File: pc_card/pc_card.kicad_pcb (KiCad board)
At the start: 4 copper layers, 64.8 x 47.5 mm, 59 parts, among them IC1 SV 3.3V, IC3 SV 4.5V, IC4 TPA152DR, J1 PCMCIA Connector, J2 Headphones Out, J3 SPI, U1 Z8601720ASG, U2 93CxxC, U3 YMF289B-S, U4 YAC516-E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

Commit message: up
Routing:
- net Net-(U3-DO): track 38.0 -> 31.5 mm
- net AGND: track 228.7 -> 234.5 mm, vias 119 -> 133
- net LRO: track 38.7 -> 40.7 mm
- net CLKO: track 33.5 -> 35.4 mm
- net BCO: track 35.0 -> 35.7 mm
- net ICS0#: track 65.7 -> 66.0 mm, vias 2 -> 3

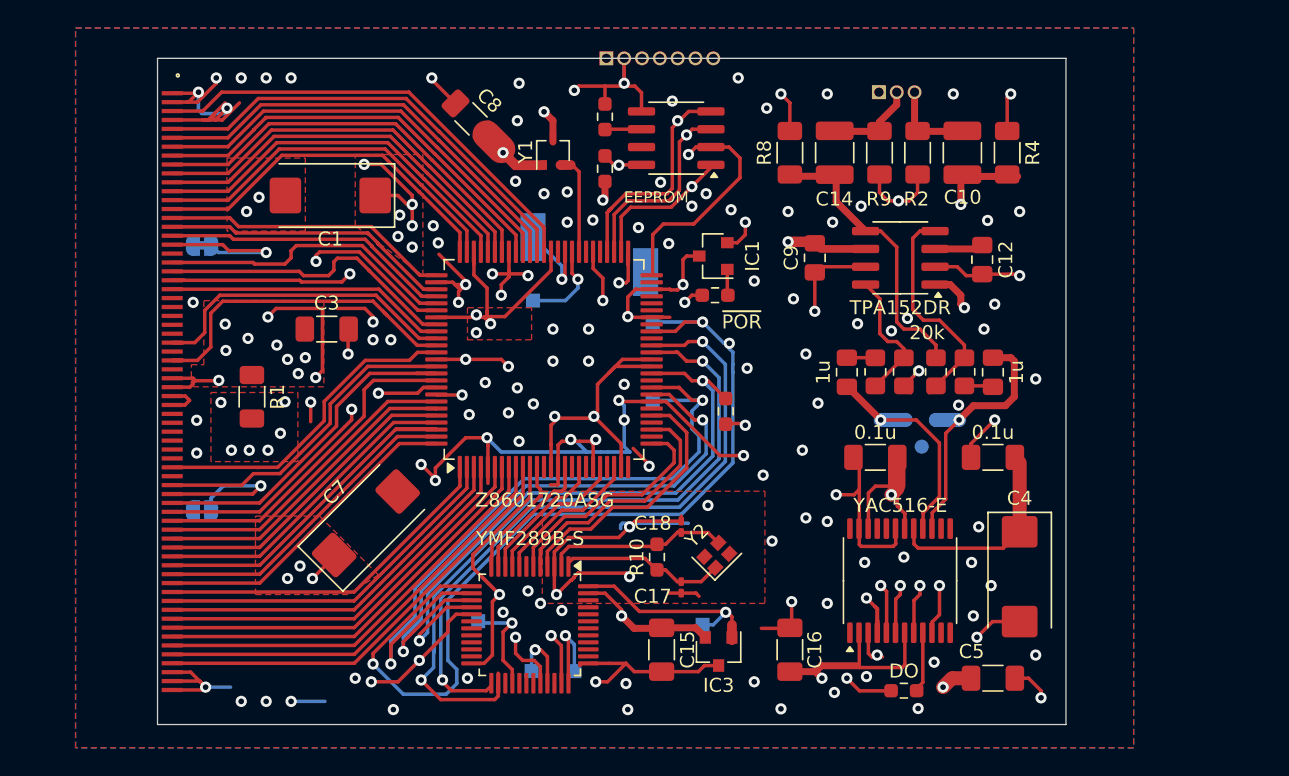
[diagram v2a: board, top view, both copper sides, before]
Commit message: hw rev3
* reDfMing the card so the connector can be assembled easier
* added software and specs
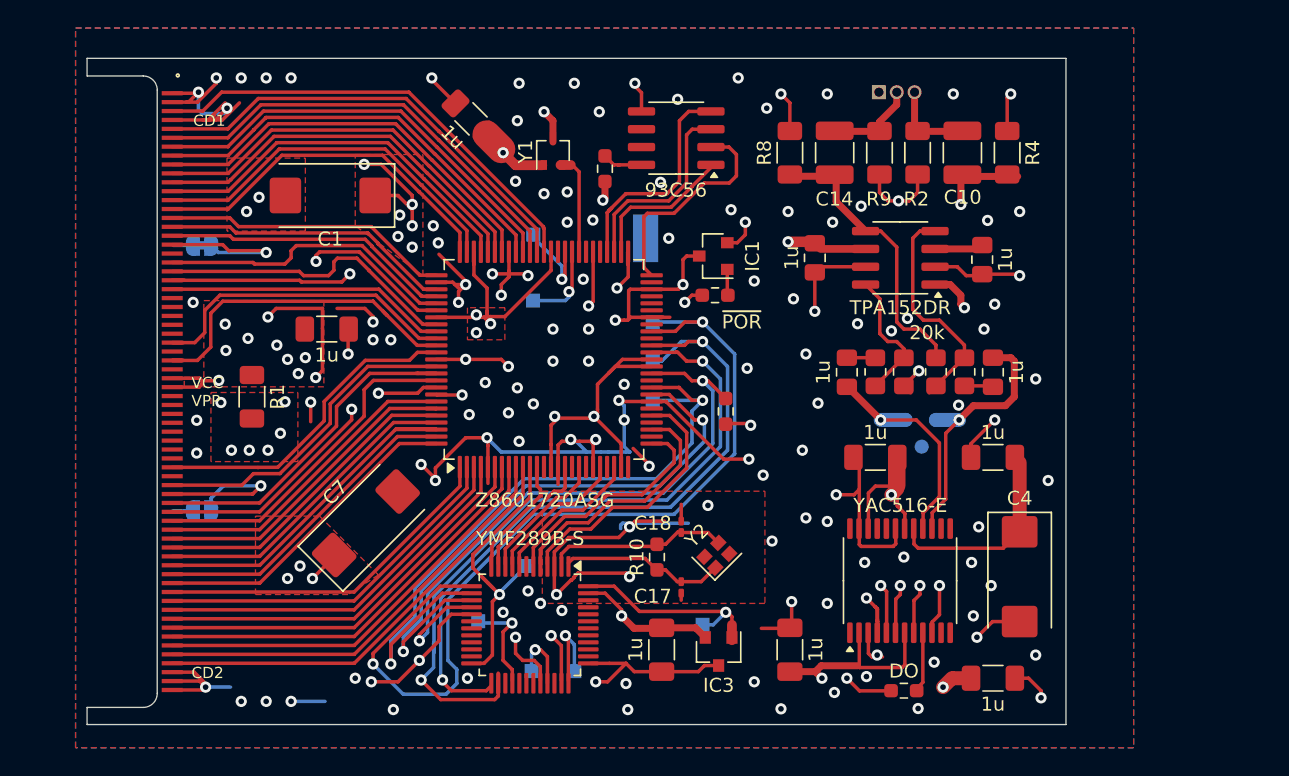
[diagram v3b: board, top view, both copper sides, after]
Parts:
- removed J3: SPI, Connector_PinHeader_1.27mm:PinHeader_1x07_P1.27mm_Vertical
- removed R13: ORG, Resistor_SMD:R_0603_1608Metric_Pad0.98x0.95mm_HandSolder
- added TP13: A0, TestPoint:TestPoint_Pad_1.0x1.0mm, B.Cu at (138.6, 78.9)
- added TP14: ~{RESET}, TestPoint:TestPoint_Pad_1.0x1.0mm, B.Cu at (129.5, 93.5)
- C15, C16, C2, C3, C5, C6, C8: value 0.1u -> 1u
- R11: value IRQ -> 20k
- TP7: footprint TestPoint:TestPoint_Keystone_5015_Micro-Minature -> TestPoint:TestPoint_Pad_1.0x1.0mm
- U2: value 93CxxC -> 93C56
- moved TP5 2.41 mm to (138.0, 70.1)
- moved TP7 0.18 mm to (130.0, 69.8)
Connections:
- U2 pad 6: Net-(U2-ORG) -> AGND
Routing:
- net POR#: track 30.1 -> 12.5 mm
- net EE_CS: track 20.5 -> 10.5 mm, vias 1 -> 0
- net AGND: track 234.5 -> 225.3 mm
- net EE_SK: track 24.2 -> 15.8 mm, vias 1 -> 0
- net VPP: track 10.4 -> 2.89 mm, vias 1 -> 0
- net EE_DO: track 20.3 -> 14.1 mm, vias 1 -> 0
- net EE_DI: track 22.0 -> 16.0 mm, vias 1 -> 0
- net IA0: track 47.2 -> 51.1 mm
- net ATA_HRESET#: track 51.8 -> 54.6 mm
- net (no net): track 2.74 -> 0.00 mm
- net Net-(U2-ORG): track 2.58 -> 0.00 mm
- net VCC: track 275.0 -> 277.3 mm
- net IRD#: track 50.6 -> 49.6 mm
- net IWR#: track 42.7 -> 42.0 mm
- net IIRQ#: track 44.7 -> 44.1 mm
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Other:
- board size 64.8 x 47.5 mm -> 69.8 x 47.5 mm
- board text added: "CD1"
- board text added: "CD2"
- board text added: "HW rev.3"
- board text added: "VCC VPP"
- board text removed: "HW rev.2"
- board text removed: "VPP GND DI DO SK CS ~{RES}"

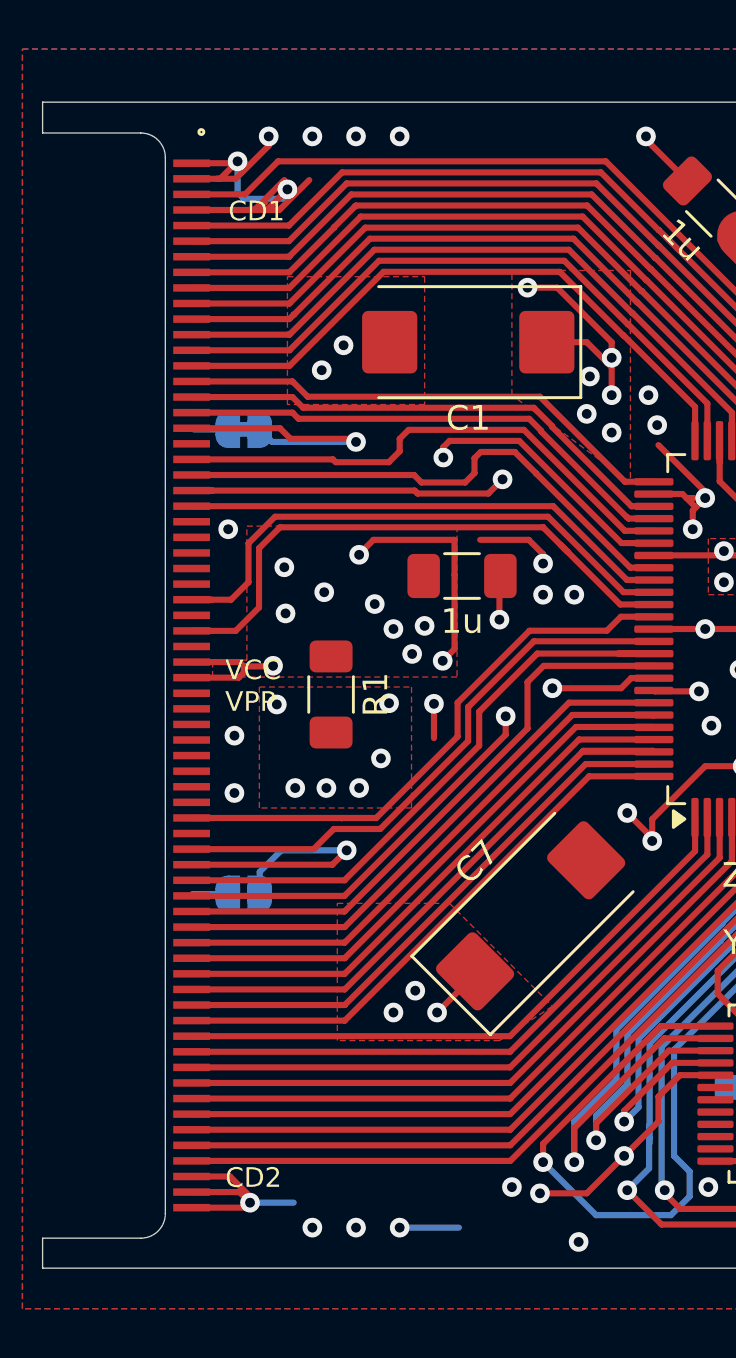
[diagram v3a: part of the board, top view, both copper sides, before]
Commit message: fiddling with connector
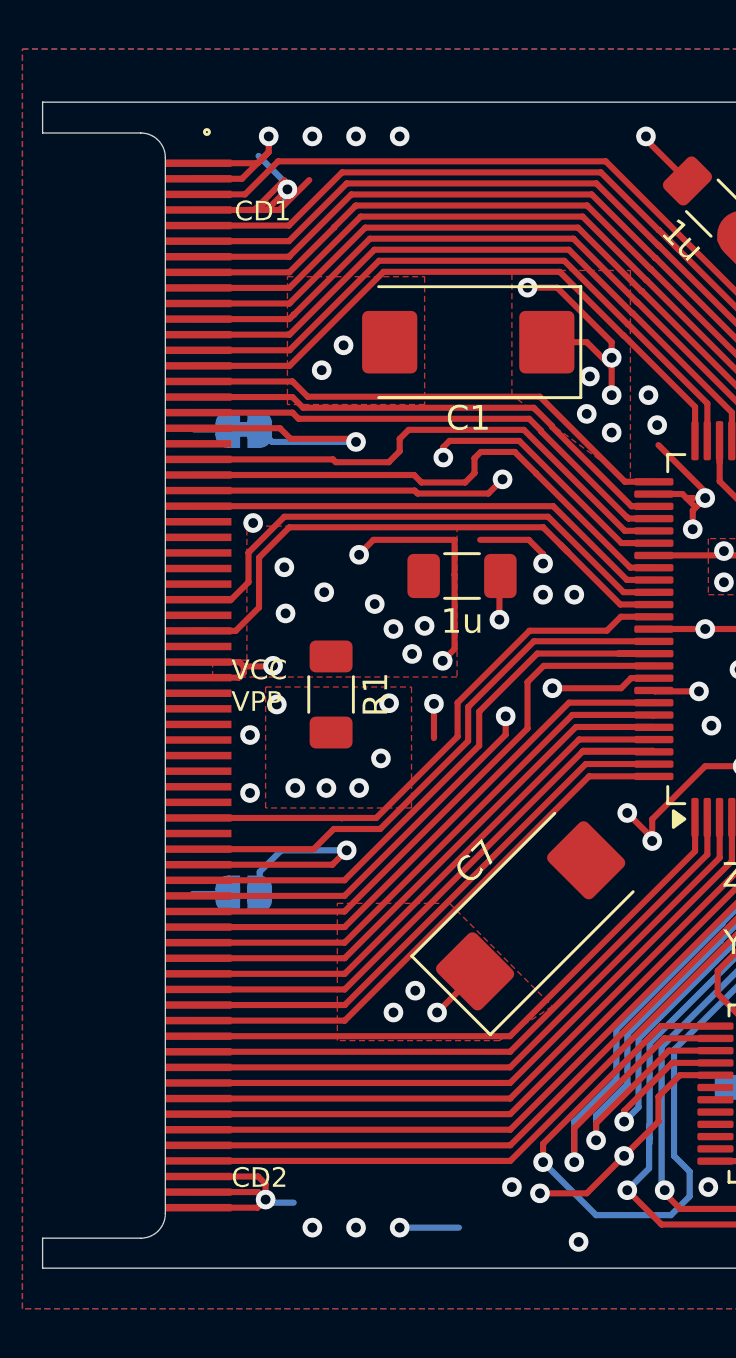
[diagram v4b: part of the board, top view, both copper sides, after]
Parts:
- moved J1 0.23 mm to (104.5, 59.8)
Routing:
- net WE#: track 23.3 -> 21.4 mm
- net AGND: track 225.3 -> 226.2 mm, vias 133 -> 132

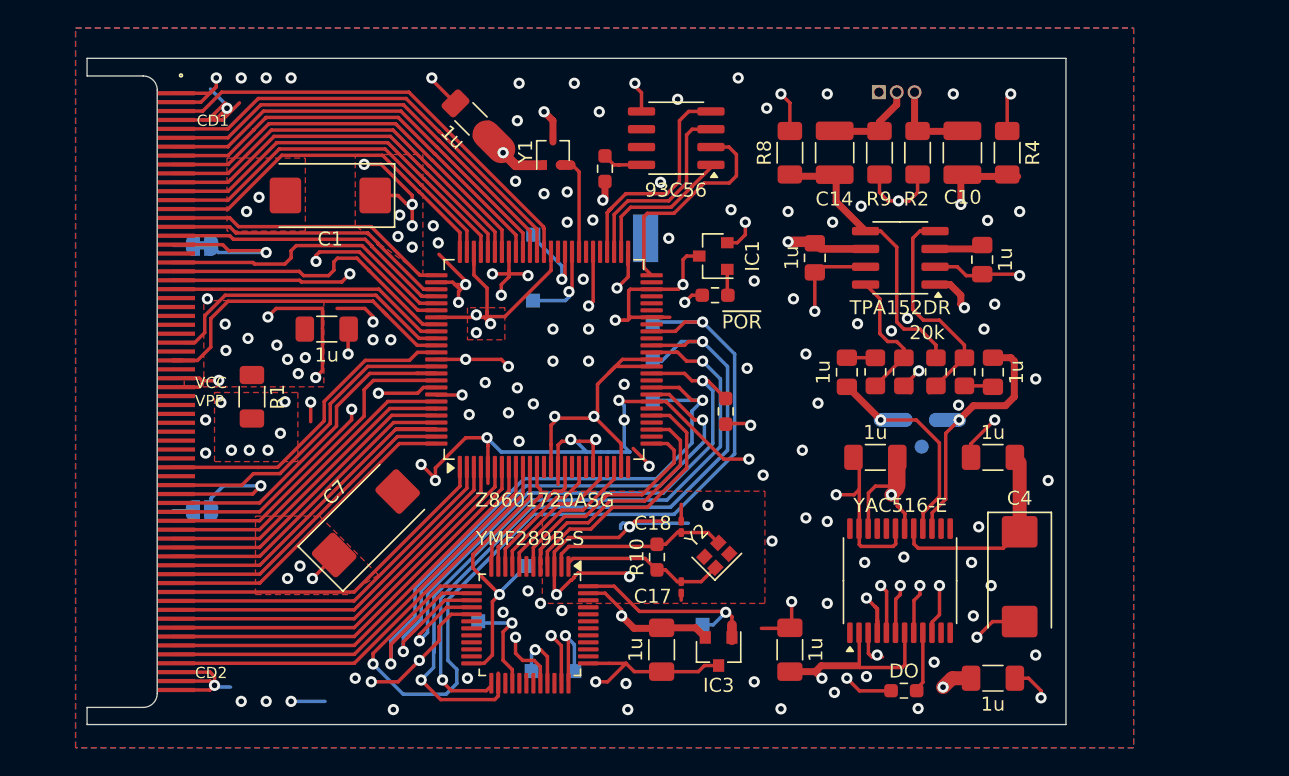
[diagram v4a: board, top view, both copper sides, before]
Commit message: socket assembly
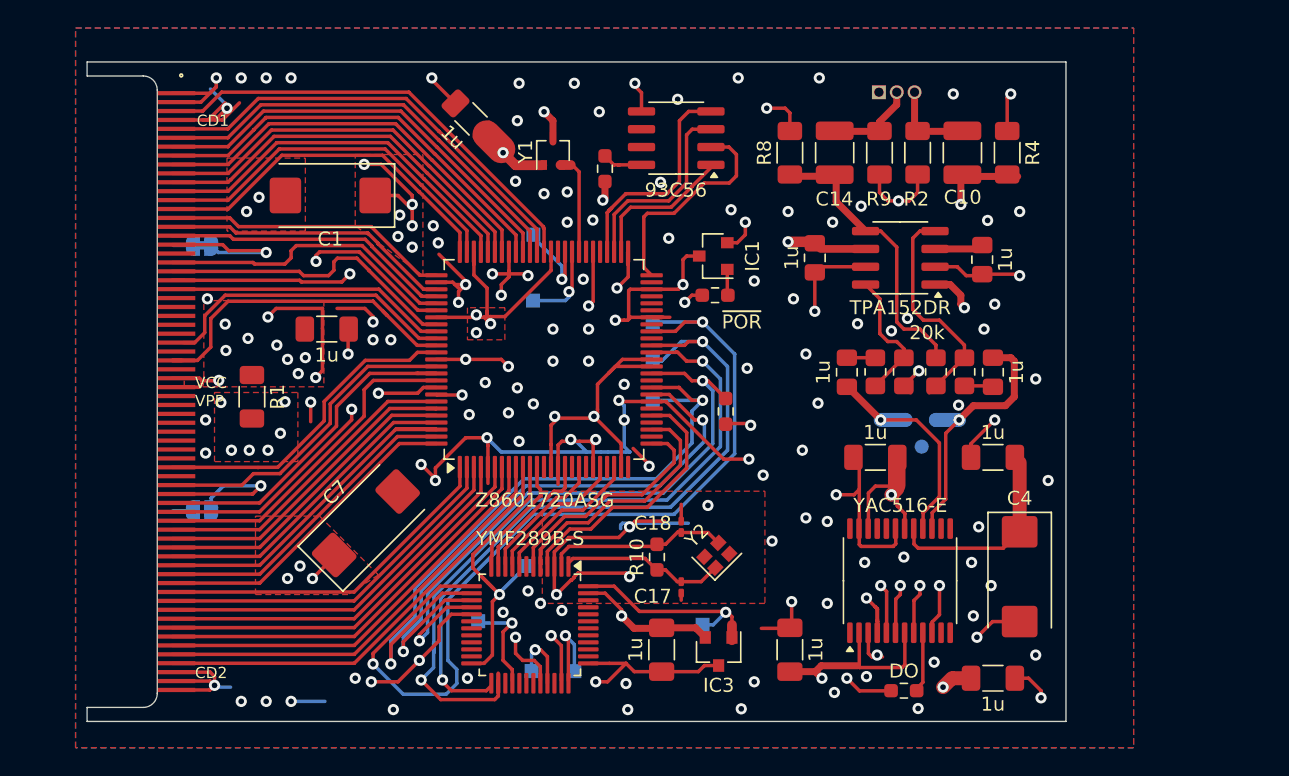
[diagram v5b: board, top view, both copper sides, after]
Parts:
- removed TP5: GND, TestPoint:TestPoint_Keystone_5015_Micro-Minature
- moved J1 21.8 mm to (99.8, 81.0)
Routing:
- net AGND: track 226.2 -> 226.3 mm, vias 132 -> 130
- net unconnected-(J1-A17-Pad46): vias 0 -> 1
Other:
- board size 69.8 x 47.5 mm -> 69.8 x 47 mm

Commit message: messing with xtal
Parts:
- Y1: value 4.19MHz -> 8MHZ
- Y2: footprint Crystal:Crystal_SMD_2016-4Pin_2.0x1.6mm -> Crystal:Crystal_SMD_2520-4Pin_2.5x2.0mm
- moved TP12 3.67 mm to (127.0, 101.0)
- moved Y2 0.18 mm to (143.0, 92.8)
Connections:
- Y2 pad 4: (no net) -> unconnected-(Y2-Pad4)
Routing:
- net AGND: track 226.3 -> 228.1 mm
- net ATA_HRESET#: track 54.6 -> 55.9 mm
- net DACPD: track 38.8 -> 37.5 mm
- net AVDD: track 155.0 -> 155.6 mm
- net LRO: track 40.7 -> 40.1 mm
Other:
- board size 69.8 x 47 mm -> 74 x 47 mm

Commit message: INF file
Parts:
- removed C5: 1u, Capacitor_SMD:C_1206_3216Metric_Pad1.33x1.80mm_HandSolder
- added H1: MountingHole, fixtures:mousebite, F.Cu at (98.2, 58.0)
- added H2: MountingHole, fixtures:mousebite, F.Cu at (98.3, 104.0)
- added R13: 100k, Resistor_SMD:R_0805_2012Metric_Pad1.20x1.40mm_HandSolder, F.Cu at (149.2, 62.2)
- added TP5: AMP, TestPoint:TestPoint_Pad_1.0x1.0mm, B.Cu at (146.9, 64.6)
- C17, C18: footprint Capacitor_SMD:C_0201_0603Metric_Pad0.64x0.40mm_HandSolder -> Capacitor_SMD:C_0603_1608Metric_Pad1.08x0.95mm_HandSolder
- J2: value Headphones Out -> Sound Out; footprint Connector_PinHeader_1.27mm:PinHeader_1x03_P1.27mm_Vertical -> SJ1-2533-SMT-TR:CUI_SJ1-2533-SMT-TR; moved to F.Cu
- moved J2 34.6 mm to (181.9, 81.0), turned to 180 degrees
- moved R2 24.7 mm to (166.5, 87.0), turned to 180 degrees
- moved C14 20.1 mm to (168.1, 75.4)
- moved R8 19.8 mm to (164.5, 75.4)
- moved R7 19.7 mm to (159.1, 60.5), turned to 0 degrees
- moved C10 19.7 mm to (168.0, 82.3), turned to 90 degrees
- moved R6 19.3 mm to (154.0, 60.5), turned to 0 degrees
- moved R4 18.3 mm to (164.5, 82.3), turned to 90 degrees
- moved R9 13.8 mm to (166.7, 70.7), turned to 180 degrees
- moved C9 13.7 mm to (162.3, 65.3), turned to -90 degrees
- moved C12 13.6 mm to (149.2, 67.1)
- moved R5 11.8 mm to (154.0, 70.0), turned to 180 degrees
- moved R3 9.67 mm to (159.3, 70.0), turned to 180 degrees
- moved C11 8.40 mm to (158.7, 87.0), turned to 0 degrees
- moved C2 8.23 mm to (163.3, 93.9), turned to -90 degrees
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- renumbered IC3 to IC2
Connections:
- net LEFT renamed AMP.LEFT
- net RIGHT renamed AMP.RIGHT
- C11 pad 1: Net-(C11-Pad1) -> AOTR
- C11 pad 2: AOTR -> Net-(C11-Pad2)
- IC4 pad 2: AGND -> MUTE
- R3 pad 1: Net-(IC4-IN2-) -> Net-(IC4-VO2)
- R3 pad 2: Net-(IC4-VO2) -> Net-(IC4-IN2-)
- R5 pad 1: Net-(C11-Pad1) -> Net-(IC4-IN2-)
- R5 pad 2: Net-(IC4-IN2-) -> Net-(C11-Pad2)
- TP1 pad 1: AOTR -> Net-(C11-Pad2)
- TP2 pad 1: AOTL -> Net-(C13-Pad1)
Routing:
- net Net-(C13-Pad1): track 2.02 -> 40.8 mm, vias 0 -> 2
- net AVDD: track 155.6 -> 129.1 mm, vias 12 -> 11
- net Net-(C11-Pad2): track 0.00 -> 21.9 mm, vias 0 -> 2
- net AOTR: track 18.9 -> 4.13 mm, vias 1 -> 0
- net AGND: track 228.1 -> 218.0 mm, vias 130 -> 128
- net AOTL: track 16.1 -> 6.11 mm, vias 1 -> 0
- net Net-(IC4-IN2-): track 16.2 -> 6.40 mm
- net Net-(U3-DO): track 31.9 -> 40.7 mm
- net MUTE: track 0.00 -> 8.66 mm, vias 0 -> 1
- net Net-(IC4-VO1): track 25.6 -> 33.0 mm, vias 3 -> 2
- net AMP.RIGHT: track 7.34 -> 13.4 mm
- net DO: track 4.38 -> 7.86 mm
- net Net-(IC4-VO2): track 20.5 -> 17.3 mm
- net Net-(IC4-IN1-): track 9.55 -> 6.40 mm
- net XO: track 12.5 -> 15.4 mm
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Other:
- board size 74 x 47 mm -> 87.8 x 47 mm
- board text added: "Breakaway connector holder"
- board text added: "OPL3 PCMCIA PC Card tilde.gay/~ai/cardbarker"
- board text removed: "Card Barker OPL3 PCMCIA PC Card tilde.gay/~ai/cardbarker"
- board text removed: "GND R L"
